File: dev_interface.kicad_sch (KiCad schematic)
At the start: 18 parts, among them U1 TLV9301xDBV, U2 ADS1014IDGS, U3 ADS1014IDGS, U4 ISO164xB, U5 DACx53401

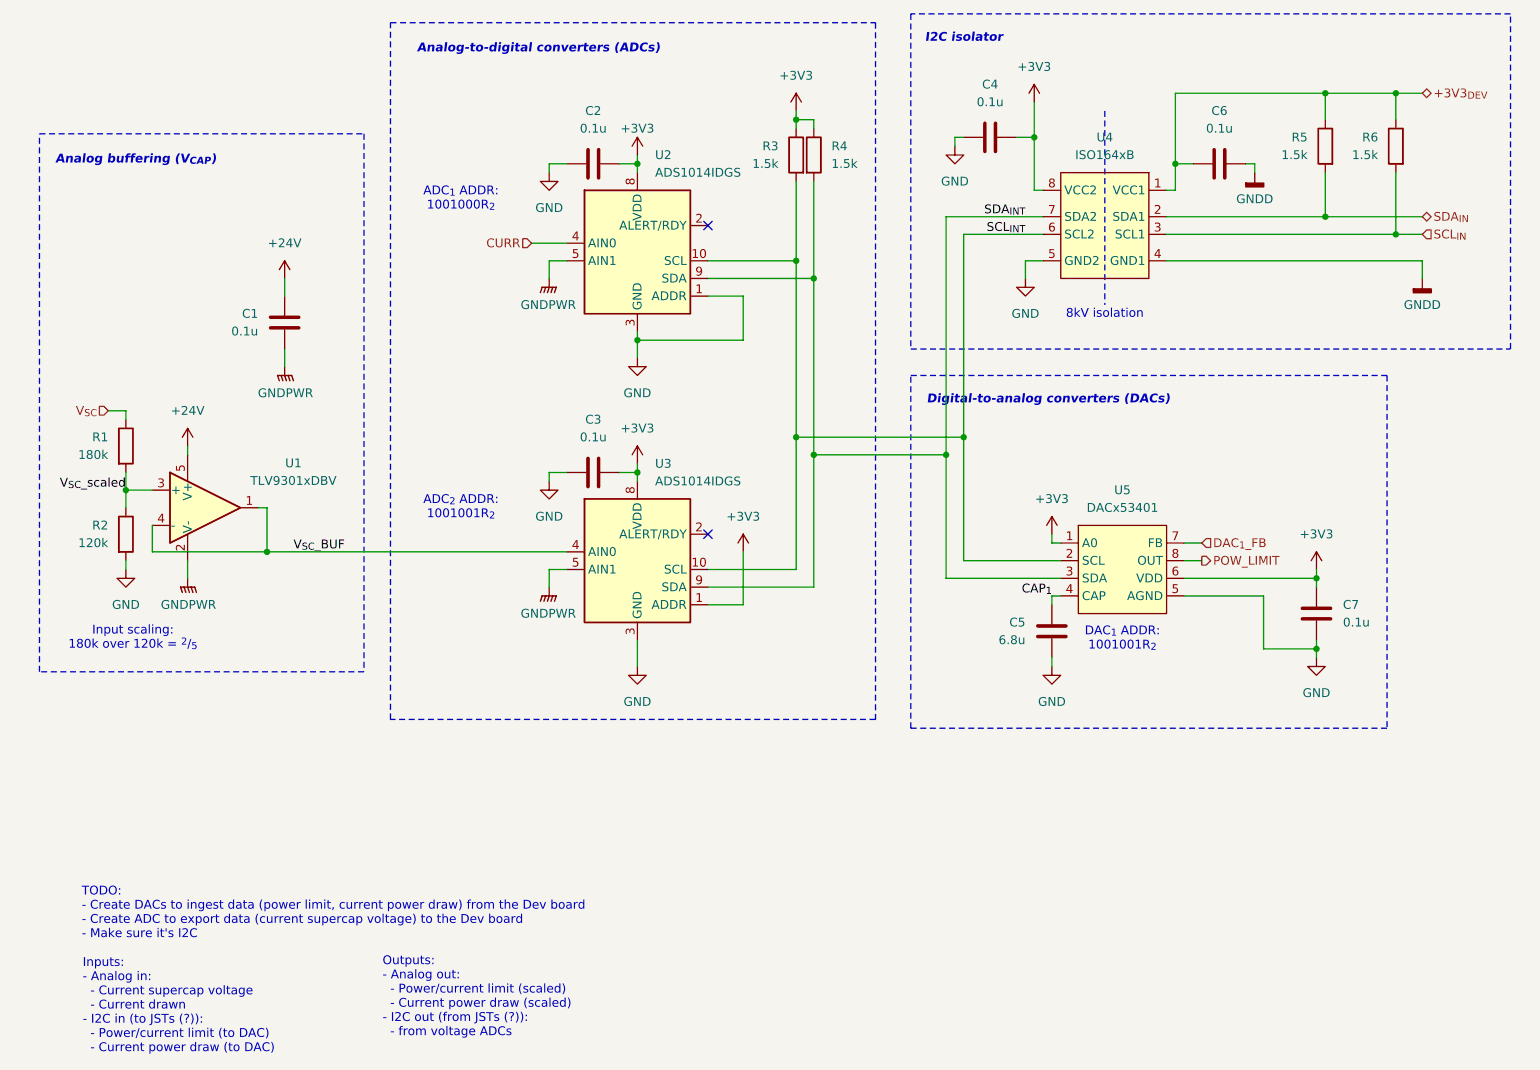
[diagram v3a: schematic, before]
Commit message: Completed stage 2 schematic
+ added SPICE models for all the custom components
+ renumbered components
+ updated library with stage 2 symbols
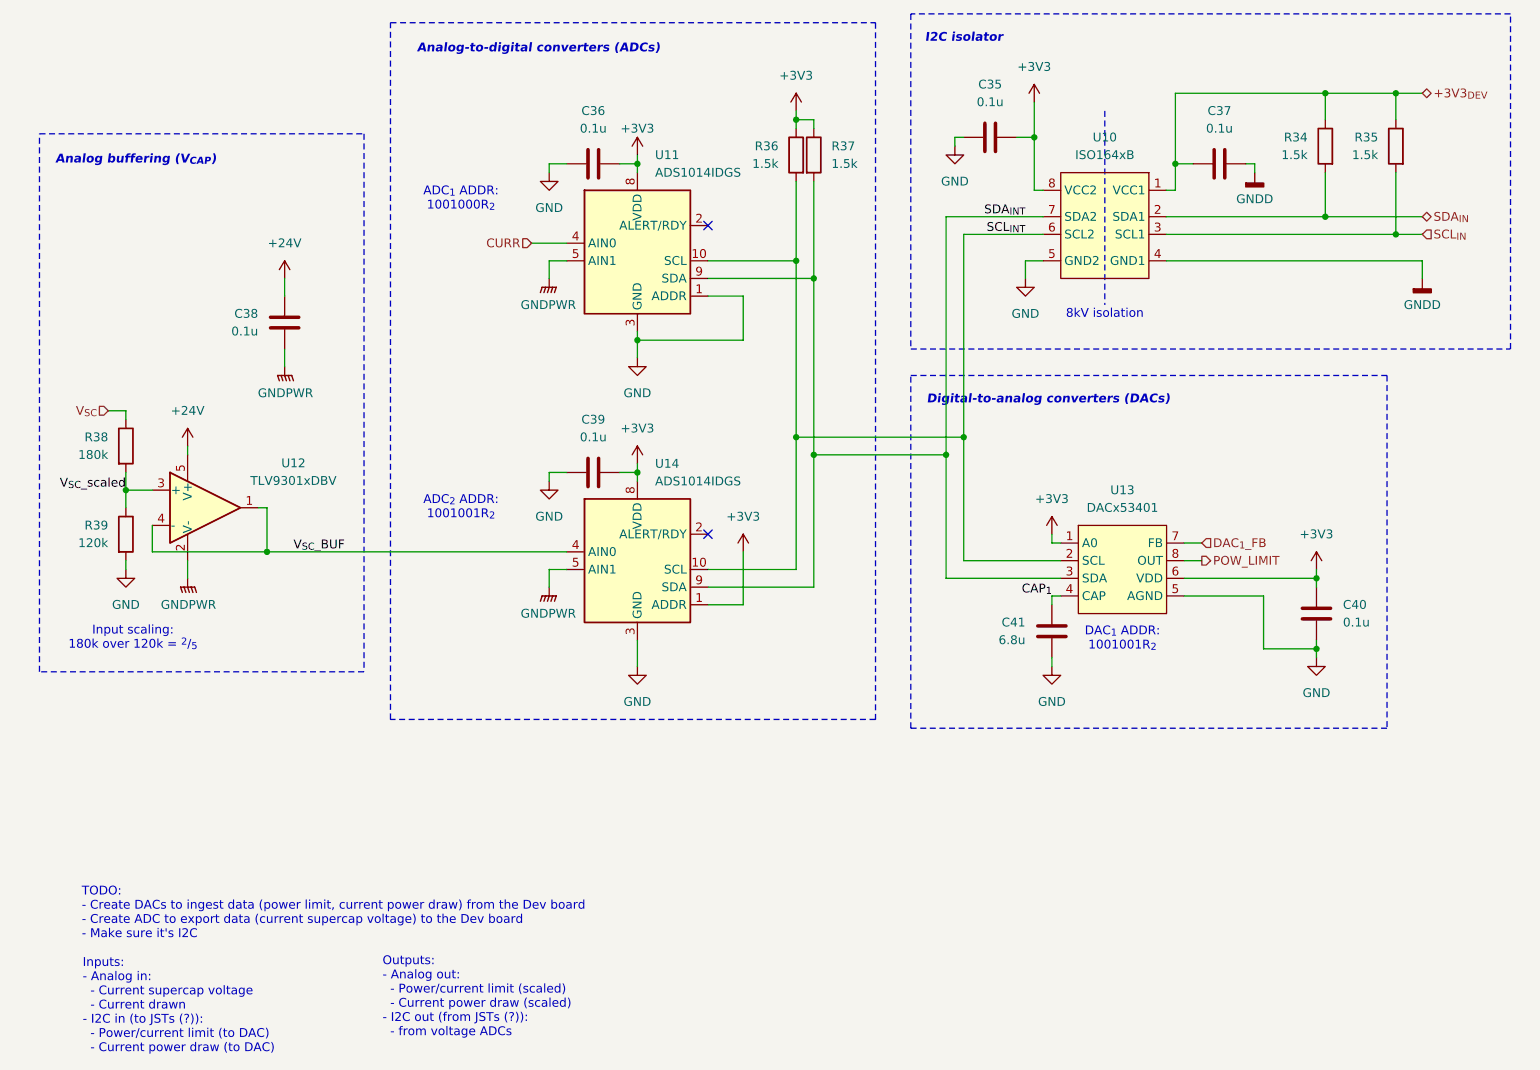
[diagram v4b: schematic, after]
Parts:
- renumbered C4 to C35, C2 to C36, C6 to C37, C1 to C38, C3 to C39, C7 to C40, C5 to C41, R5 to R34, R6 to R35, R3 to R36, R4 to R37, R1 to R38, R2 to R39, U4 to U10, U2 to U11, U1 to U12, U5 to U13, U3 to U14
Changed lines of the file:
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@@
 		(on_board yes)
 		(dnp no)
-		(property "Reference" "U3"
+		(property "Reference" "U14"
 			(at 132.08 104.14 0)
 			(effects
@@
 		(dnp no)
 		(fields_autoplaced yes)
-		(property "Reference" "#PWR0104"
+		(property "Reference" "#PWR068"
 			(at 185.42 83.82 0)
 			(effects
@@
 		(dnp no)
 		(fields_autoplaced yes)
-		(property "Reference" "#PWR0115"
+		(property "Reference" "#PWR082"
 			(at 129.54 139.7 0)
 			(effects
@@
 		(dnp no)
 		(fields_autoplaced yes)
-		(property "Reference" "#PWR0122"
+		(property "Reference" "#PWR070"
 			(at 129.54 95.25 0)
 			(effects
@@
 		(dnp no)
 		(fields_autoplaced yes)
-		(property "Reference" "C6"
+		(property "Reference" "C37"
 			(at 213.36 53.34 90)
 			(effects
@@
 		(dnp no)
 		(fields_autoplaced yes)
-		(property "Reference" "#PWR0101"
+		(property "Reference" "#PWR065"
 			(at 218.44 68.58 0)
 			(effects
@@
 		(dnp no)
 		(fields_autoplaced yes)
-		(property "Reference" "#PWR0116"
+		(property "Reference" "#PWR061"
 			(at 152.4 57.15 0)
 			(effects
@@
 		(dnp no)
 		(fields_autoplaced yes)
-		(property "Reference" "R3"
+		(property "Reference" "R36"
 			(at 149.86 58.4199 0)
 			(effects
@@
 		(dnp no)
 		(fields_autoplaced yes)
-		(property "Reference" "#PWR0111"
+		(property "Reference" "#PWR064"
 			(at 116.84 68.58 0)
 			(effects
@@
 		(on_board yes)
 		(dnp no)
-		(property "Reference" "#PWR0117"
+		(property "Reference" "#PWR063"
 			(at 129.54 63.5 0)
 			(effects
@@
 		(dnp no)
 		(fields_autoplaced yes)
-		(property "Reference" "U5"
+		(property "Reference" "U13"
 			(at 199.39 107.95 0)
 			(effects
@@
 		(on_board yes)
 		(dnp no)
-		(property "Reference" "C5"
+		(property "Reference" "C41"
 			(at 185.42 126.9999 0)
 			(effects
@@
 		(on_board yes)
 		(dnp no)
-		(property "Reference" "C1"
+		(property "Reference" "C38"
 			(at 74.93 82.5499 0)
 			(effects
@@
 		(dnp no)
 		(fields_autoplaced yes)
-		(property "Reference" "C4"
+		(property "Reference" "C35"
 			(at 180.34 49.53 90)
 			(effects
@@
 		(dnp no)
 		(fields_autoplaced yes)
-		(property "Reference" "#PWR0124"
+		(property "Reference" "#PWR073"
 			(at 129.54 107.95 0)
 			(effects
@@
 		(on_board yes)
 		(dnp no)
-		(property "Reference" "U2"
+		(property "Reference" "U11"
 			(at 132.08 59.69 0)
 			(effects
@@
 		(dnp no)
 		(fields_autoplaced yes)
-		(property "Reference" "#PWR0108"
+		(property "Reference" "#PWR072"
 			(at 64.77 105.41 0)
 			(effects
@@
 		(on_board yes)
 		(dnp no)
-		(property "Reference" "R4"
+		(property "Reference" "R37"
 			(at 157.48 58.4199 0)
 			(effects
@@
 		(dnp no)
 		(fields_autoplaced yes)
-		(property "Reference" "#PWR0107"
+		(property "Reference" "#PWR071"
 			(at 78.74 95.25 0)
 			(effects
@@
 		(dnp no)
 		(fields_autoplaced yes)
-		(property "Reference" "#PWR0123"
+		(property "Reference" "#PWR076"
 			(at 144.78 120.65 0)
 			(effects
@@
 		(dnp no)
 		(fields_autoplaced yes)
-		(property "Reference" "#PWR0109"
+		(property "Reference" "#PWR066"
 			(at 78.74 81.28 0)
 			(effects
@@
 		(dnp no)
 		(fields_autoplaced yes)
-		(property "Reference" "#PWR0121"
+		(property "Reference" "#PWR078"
 			(at 227.33 123.19 0)
 			(effects
@@
 		(dnp no)
 		(fields_autoplaced yes)
-		(property "Reference" "#PWR0118"
+		(property "Reference" "#PWR075"
 			(at 189.23 118.11 0)
 			(effects
@@
 		(dnp no)
 		(fields_autoplaced yes)
-		(property "Reference" "#PWR0119"
+		(property "Reference" "#PWR083"
 			(at 189.23 139.7 0)
 			(effects
@@
 		(dnp no)
 		(fields_autoplaced yes)
-		(property "Reference" "U1"
+		(property "Reference" "U12"
 			(at 80.01 104.0698 0)
 			(effects
@@
 		(dnp no)
 		(fields_autoplaced yes)
-		(property "Reference" "C3"
+		(property "Reference" "C39"
 			(at 123.19 97.79 90)
 			(effects
@@
 		(dnp no)
 		(fields_autoplaced yes)
-		(property "Reference" "#PWR0103"
+		(property "Reference" "#PWR062"
 			(at 175.26 64.77 0)
 			(effects
@@
 		(dnp no)
 		(fields_autoplaced yes)
-		(property "Reference" "R5"
+		(property "Reference" "R34"
 			(at 226.06 57.1499 0)
 			(effects
@@
 		(dnp no)
 		(fields_autoplaced yes)
-		(property "Reference" "#PWR0106"
+		(property "Reference" "#PWR077"
 			(at 55.88 125.73 0)
 			(effects
@@
 		(on_board yes)
 		(dnp no)
-		(property "Reference" "R2"
+		(property "Reference" "R39"
 			(at 53.34 113.0299 0)
 			(effects
@@
 		(on_board yes)
 		(dnp no)
-		(property "Reference" "R1"
+		(property "Reference" "R38"
 			(at 53.34 100.3299 0)
 			(effects
@@
 		(dnp no)
 		(fields_autoplaced yes)
-		(property "Reference" "#PWR0105"
+		(property "Reference" "#PWR060"
 			(at 186.69 55.88 0)
 			(effects
@@
 		(on_board yes)
 		(dnp no)
-		(property "Reference" "U4"
+		(property "Reference" "U10"
 			(at 196.85 57.15 0)
 			(effects
@@
 		(dnp no)
 		(fields_autoplaced yes)
-		(property "Reference" "#PWR0113"
+		(property "Reference" "#PWR074"
 			(at 116.84 113.03 0)
 			(effects
@@
 		(dnp no)
 		(fields_autoplaced yes)
-		(property "Reference" "#PWR0120"
+		(property "Reference" "#PWR081"
 			(at 227.33 138.43 0)
 			(effects
@@
 		(dnp no)
 		(fields_autoplaced yes)
-		(property "Reference" "#PWR0102"
+		(property "Reference" "#PWR069"
 			(at 242.57 83.82 0)
 			(effects
@@
 		(dnp no)
 		(fields_autoplaced yes)
-		(property "Reference" "#PWR0112"
+		(property "Reference" "#PWR067"
 			(at 116.84 82.55 0)
 			(effects
@@
 		(dnp no)
 		(fields_autoplaced yes)
-		(property "Reference" "C7"
+		(property "Reference" "C40"
 			(at 231.14 124.4599 0)
 			(effects
@@
 		(dnp no)
 		(fields_autoplaced yes)
-		(property "Reference" "C2"
+		(property "Reference" "C36"
 			(at 123.19 53.34 90)
 			(effects
@@
 		(dnp no)
 		(fields_autoplaced yes)
-		(property "Reference" "R6"
+		(property "Reference" "R35"
 			(at 236.22 57.1499 0)
 			(effects
@@
 		(dnp no)
 		(fields_autoplaced yes)
-		(property "Reference" "#PWR0110"
+		(property "Reference" "#PWR079"
 			(at 64.77 125.73 0)
 			(effects
@@
 		(dnp no)
 		(fields_autoplaced yes)
-		(property "Reference" "#PWR0114"
+		(property "Reference" "#PWR080"
 			(at 116.84 127 0)
 			(effects

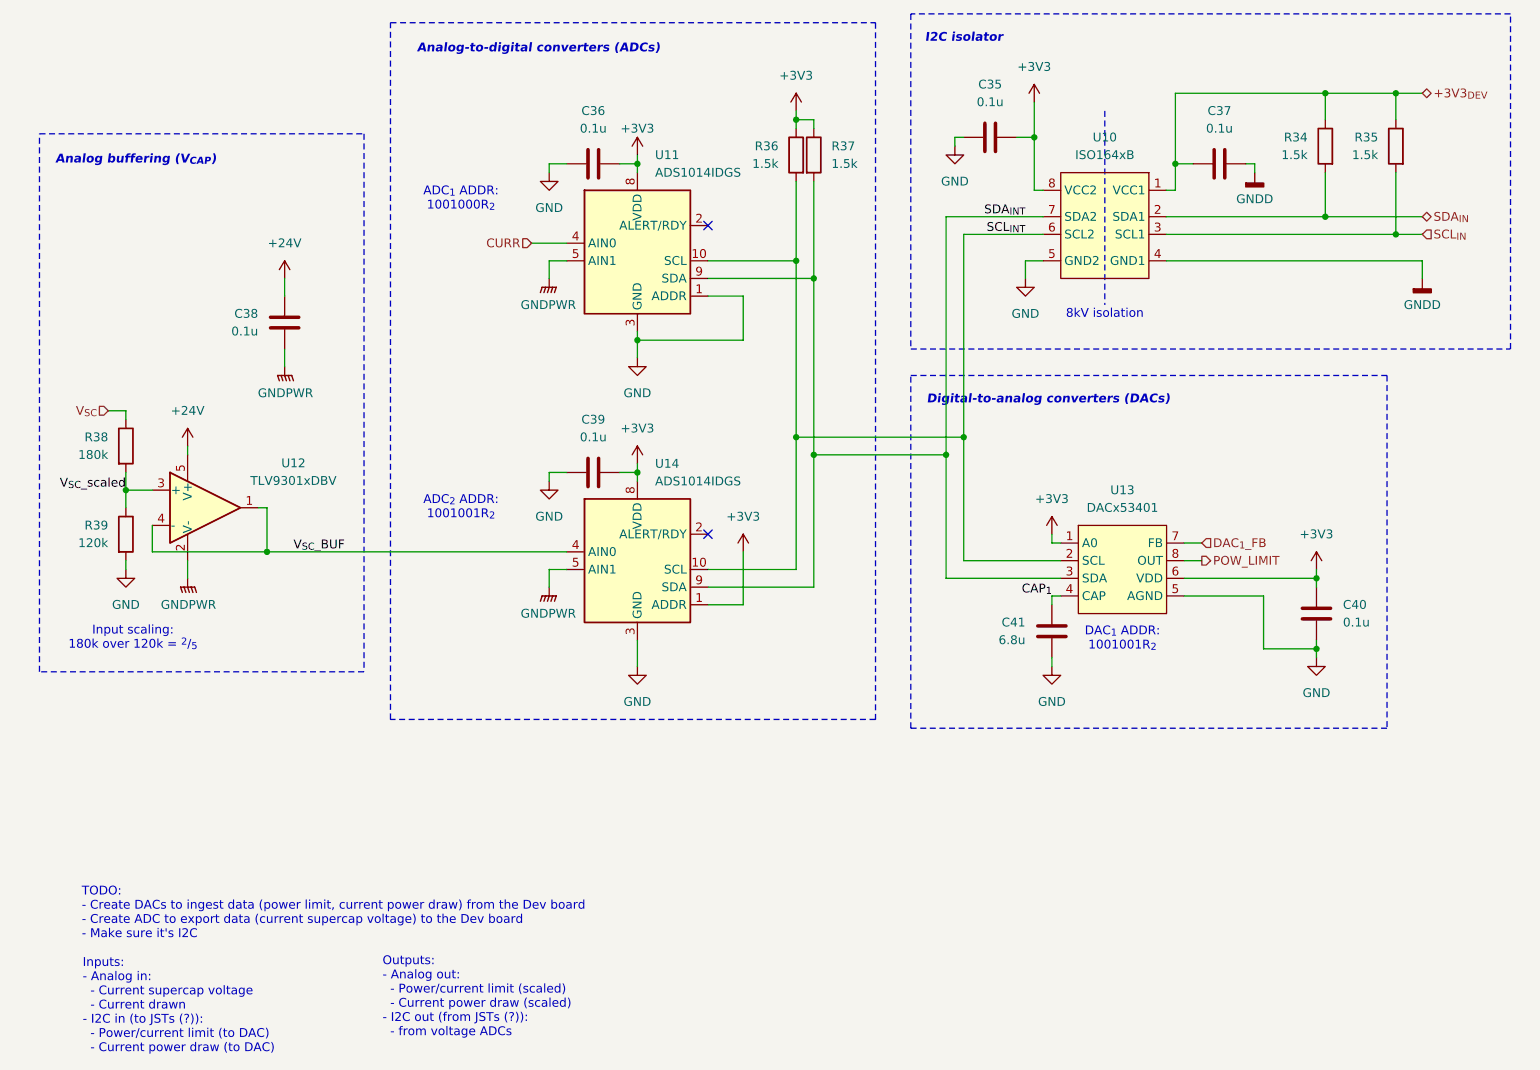
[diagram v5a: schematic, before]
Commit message: Update Mouser part numbers
Some resistors will be wrong, please check
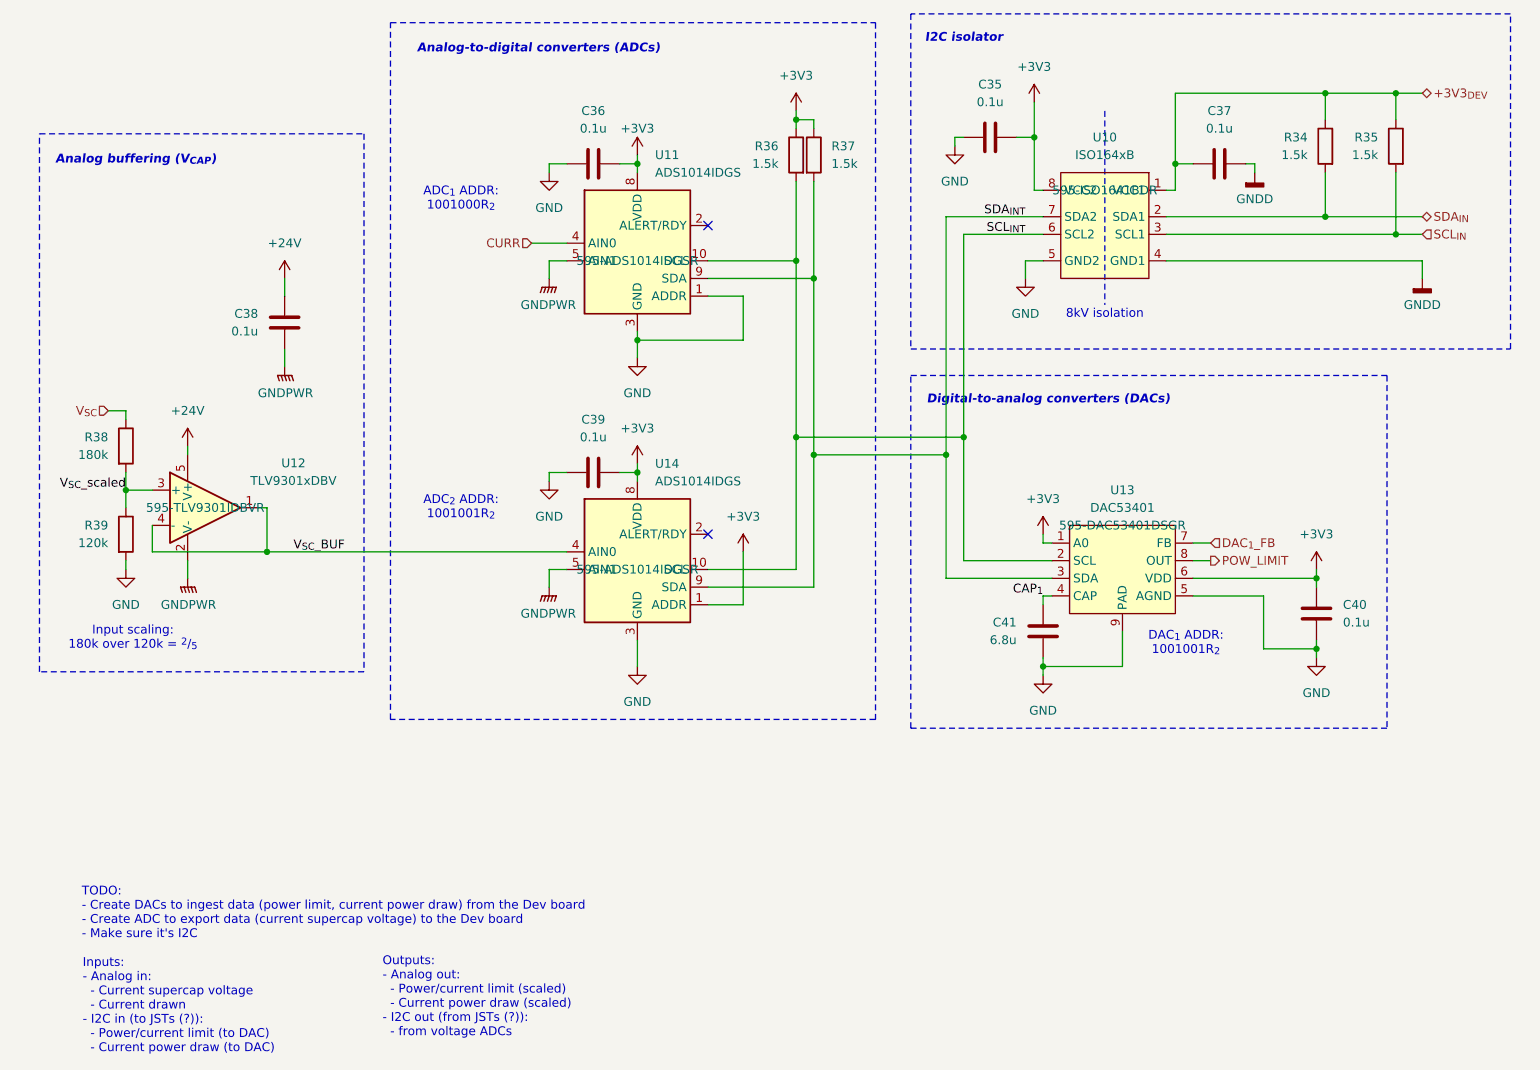
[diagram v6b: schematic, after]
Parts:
- U10: Mouser Part Number (none) -> 595-ISO1641BDR
- U11, U14: Mouser Part Number (none) -> 595-ADS1014IDGSR
- U12: Mouser Part Number (none) -> 595-TLV9301IDBVR
- U13: value DACx53401 -> DAC53401; Mouser Part Number (none) -> 595-DAC53401DSGR
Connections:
- net GND: now also U13.9 (PAD)
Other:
- moved on the sheet: C41
